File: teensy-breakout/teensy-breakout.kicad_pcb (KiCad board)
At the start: 6 copper layers, 240.5 x 168.5 mm, 103 parts, among them J1 USB_B, J10 1988820, J11 1988817, J12 1988817, J13 1988817, J14 1988817, J15 1988820, J17 1988956, J18 1988817, J19 1989010, J2 1988820, J20 1989010, J21 1988956, J22 1988817, J3 1988820, J4 1988820, J5 1988820, J6 1988820, J7 1988820, J8 1988833, J9 1988956, Q1 IRL530NSTRLPBF, SW1 7101MD9AQE, U1 Teensy4.1, U10 LSF0102DCUR, U3 FT232RL, U6 ICL7667CBAZA-TDKR, U7 LSF0102DCUR, U8 LSF0102DCUR

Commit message: Final silkscreen & testpoint touchups (still no images tho)
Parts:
- removed the REF** at (173.7, 121.1)
- added REF**: TestPoint_Pad_D1.5mm, TestPoint:TestPoint_Pad_D1.5mm, F.Cu at (94.0, 109.2)
- added REF**: PinHeader_1x02_P2.54mm_Vertical, Connector_PinHeader_2.54mm:PinHeader_1x02_P2.54mm_Vertical, F.Cu at (127.0, 179.1)
- added REF**: TestPoint_Pad_D1.5mm, TestPoint:TestPoint_Pad_D1.5mm, F.Cu at (78.7, 119.4)
- added REF**: TestPoint_Pad_D1.5mm, TestPoint:TestPoint_Pad_D1.5mm, F.Cu at (50.8, 119.4)
- added REF**: TestPoint_Pad_D1.5mm, TestPoint:TestPoint_Pad_D1.5mm, F.Cu at (185.4, 114.3)
- added REF**: TestPoint_Pad_D1.5mm, TestPoint:TestPoint_Pad_D1.5mm, F.Cu at (167.6, 114.3)
- added REF**: TestPoint_Pad_D1.5mm, TestPoint:TestPoint_Pad_D1.5mm, F.Cu at (45.7, 119.4)
- added REF**: TestPoint_Pad_D1.5mm, TestPoint:TestPoint_Pad_D1.5mm, F.Cu at (165.1, 114.3)
- added REF**: TestPoint_Pad_D1.5mm, TestPoint:TestPoint_Pad_D1.5mm, F.Cu at (182.9, 114.3)
- added REF**: TestPoint_Pad_D1.5mm, TestPoint:TestPoint_Pad_D1.5mm, F.Cu at (193.0, 114.3)
- added REF**: TestPoint_Pad_D1.5mm, TestPoint:TestPoint_Pad_D1.5mm, F.Cu at (200.7, 114.3)
- added REF**: TestPoint_Pad_D1.5mm, TestPoint:TestPoint_Pad_D1.5mm, F.Cu at (195.6, 114.3)
- added REF**: TestPoint_Pad_D1.5mm, TestPoint:TestPoint_Pad_D1.5mm, F.Cu at (71.1, 119.4)
- added REF**: TestPoint_Pad_D1.5mm, TestPoint:TestPoint_Pad_D1.5mm, F.Cu at (55.9, 119.4)
- added REF**: TestPoint_Pad_D1.5mm, TestPoint:TestPoint_Pad_D1.5mm, F.Cu at (188.0, 114.3)
- added REF**: TestPoint_Pad_D1.5mm, TestPoint:TestPoint_Pad_D1.5mm, F.Cu at (129.5, 175.3)
- added REF**: TestPoint_Pad_D1.5mm, TestPoint:TestPoint_Pad_D1.5mm, F.Cu at (160.0, 114.3)
- added REF**: TestPoint_Pad_D1.5mm, TestPoint:TestPoint_Pad_D1.5mm, F.Cu at (203.2, 114.3)
- added REF**: TestPoint_Pad_D1.5mm, TestPoint:TestPoint_Pad_D1.5mm, F.Cu at (81.3, 119.4)
- added REF**: TestPoint_Pad_D1.5mm, TestPoint:TestPoint_Pad_D1.5mm, F.Cu at (96.5, 109.2)
- added REF**: PinHeader_1x24_P2.54mm_Vertical, Connector_PinHeader_2.54mm:PinHeader_1x24_P2.54mm_Vertical, F.Cu at (147.4, 117.4)
- added REF**: TestPoint_Pad_D1.5mm, TestPoint:TestPoint_Pad_D1.5mm, F.Cu at (38.1, 119.4)
- added REF**: PinHeader_1x24_P2.54mm_Vertical, Connector_PinHeader_2.54mm:PinHeader_1x24_P2.54mm_Vertical, F.Cu at (38.1, 114.8)
- added REF**: TestPoint_Pad_D1.5mm, TestPoint:TestPoint_Pad_D1.5mm, F.Cu at (48.3, 119.4)
- added REF**: TestPoint_Pad_D1.5mm, TestPoint:TestPoint_Pad_D1.5mm, F.Cu at (88.9, 119.4)
- added REF**: TestPoint_Pad_D1.5mm, TestPoint:TestPoint_Pad_D1.5mm, F.Cu at (127.0, 175.3)
- added REF**: TestPoint_Pad_D1.5mm, TestPoint:TestPoint_Pad_D1.5mm, F.Cu at (154.9, 114.3)
- added REF**: TestPoint_Pad_D1.5mm, TestPoint:TestPoint_Pad_D1.5mm, F.Cu at (205.7, 114.3)
- added REF**: TestPoint_Pad_D1.5mm, TestPoint:TestPoint_Pad_D1.5mm, F.Cu at (83.8, 119.4)
- added REF**: TestPoint_Pad_D1.5mm, TestPoint:TestPoint_Pad_D1.5mm, F.Cu at (43.2, 119.4)
- added REF**: TestPoint_Pad_D1.5mm, TestPoint:TestPoint_Pad_D1.5mm, F.Cu at (152.4, 114.3)
- added REF**: TestPoint_Pad_D1.5mm, TestPoint:TestPoint_Pad_D1.5mm, F.Cu at (170.2, 114.3)
- added REF**: TestPoint_Pad_D1.5mm, TestPoint:TestPoint_Pad_D1.5mm, F.Cu at (73.7, 119.4)
- added REF**: TestPoint_Pad_D1.5mm, TestPoint:TestPoint_Pad_D1.5mm, F.Cu at (66.0, 119.4)
- added REF**: TestPoint_Pad_D1.5mm, TestPoint:TestPoint_Pad_D1.5mm, F.Cu at (58.4, 119.4)
- added REF**: TestPoint_Pad_D1.5mm, TestPoint:TestPoint_Pad_D1.5mm, F.Cu at (172.7, 114.3)
- added REF**: TestPoint_Pad_D1.5mm, TestPoint:TestPoint_Pad_D1.5mm, F.Cu at (198.1, 114.3)
- added REF**: TestPoint_Pad_D1.5mm, TestPoint:TestPoint_Pad_D1.5mm, F.Cu at (180.3, 114.3)
- added REF**: TestPoint_Pad_D1.5mm, TestPoint:TestPoint_Pad_D1.5mm, F.Cu at (149.9, 114.3)
- added REF**: TestPoint_Pad_D1.5mm, TestPoint:TestPoint_Pad_D1.5mm, F.Cu at (162.6, 114.3)
- added REF**: TestPoint_Pad_D1.5mm, TestPoint:TestPoint_Pad_D1.5mm, F.Cu at (91.4, 119.4)
- added REF**: TestPoint_Pad_D1.5mm, TestPoint:TestPoint_Pad_D1.5mm, F.Cu at (147.3, 114.3)
- added REF**: TestPoint_Pad_D1.5mm, TestPoint:TestPoint_Pad_D1.5mm, F.Cu at (53.3, 119.4)
- added REF**: TestPoint_Pad_D1.5mm, TestPoint:TestPoint_Pad_D1.5mm, F.Cu at (40.6, 119.4)
- added REF**: TestPoint_Pad_D1.5mm, TestPoint:TestPoint_Pad_D1.5mm, F.Cu at (177.8, 114.3)
- added REF**: TestPoint_Pad_D1.5mm, TestPoint:TestPoint_Pad_D1.5mm, F.Cu at (76.2, 119.4)
- added REF**: TestPoint_Pad_D1.5mm, TestPoint:TestPoint_Pad_D1.5mm, F.Cu at (175.3, 114.3)
- added REF**: TestPoint_Pad_D1.5mm, TestPoint:TestPoint_Pad_D1.5mm, F.Cu at (157.5, 114.3)
- added REF**: TestPoint_Pad_D1.5mm, TestPoint:TestPoint_Pad_D1.5mm, F.Cu at (61.0, 119.4)
- added REF**: TestPoint_Pad_D1.5mm, TestPoint:TestPoint_Pad_D1.5mm, F.Cu at (190.5, 114.3)
- added REF**: TestPoint_Pad_D1.5mm, TestPoint:TestPoint_Pad_D1.5mm, F.Cu at (68.6, 119.4)
- added REF**: TestPoint_Pad_D1.5mm, TestPoint:TestPoint_Pad_D1.5mm, F.Cu at (86.4, 119.4)
- added REF**: TestPoint_Pad_D1.5mm, TestPoint:TestPoint_Pad_D1.5mm, F.Cu at (63.5, 119.4)
- moved C12 15.9 mm to (44.5, 61.1), turned to -90 degrees
- moved C7 14.8 mm to (156.0, 96.7)
- moved C13 13.9 mm to (46.6, 61.0), turned to -90 degrees
- moved C20 7.92 mm to (156.0, 99.1)
- moved C9 7.75 mm to (45.6, 64.1)
- moved C23 3.30 mm to (125.2, 167.4)
- moved J5 0.23 mm to (16.6, 113.7)
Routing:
- net GND: track 737.3 -> 722.9 mm, vias 21 -> 16
- net Net-(D1-K): track 25.1 -> 37.5 mm
- net /LIM_R: track 148.6 -> 157.2 mm, vias 2 -> 1
- net /LIM_L: track 145.0 -> 153.6 mm, vias 2 -> 1
- net /UART1 CTS: track 185.8 -> 194.2 mm, vias 5 -> 4
- net /J0_4: track 190.4 -> 198.2 mm, vias 3 -> 2
- net /UART1 TX: track 196.3 -> 203.9 mm, vias 3 -> 2
- net /SCK1: track 224.1 -> 231.7 mm, vias 3 -> 2
- net /RF_CS: track 241.0 -> 248.6 mm, vias 3 -> 2
- net /NP3: track 231.0 -> 238.7 mm, vias 1 -> 0
- net /NP2: track 142.5 -> 150.1 mm, vias 3 -> 2
- net /MOSI1: track 220.4 -> 228.1 mm, vias 4 -> 3
- net /J0_3: track 198.7 -> 206.3 mm, vias 3 -> 2
- net /J0_2: track 222.0 -> 229.6 mm, vias 3 -> 2
- net /J0_1: track 223.4 -> 231.0 mm, vias 3 -> 2
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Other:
- board text added: "0"
- board text added: "1"
- board text added: "10"
- board text added: "14"
- board text added: "15"
- board text added: "18"
- board text added: "19"
- board text added: "2"
- board text added: "20"
- board text added: "22"
- board text added: "3"
- board text added: "34"
- board text added: "35"
- board text added: "36"
- board text added: "37"
- board text added: "40"
- board text added: "41"
- board text added: "9"
- board text added: "CS"
- board text added: "G0"
- board text added: "GPS Serial"
- board text added: "RST"
- board text added: "RX"
- board text added: "TX"

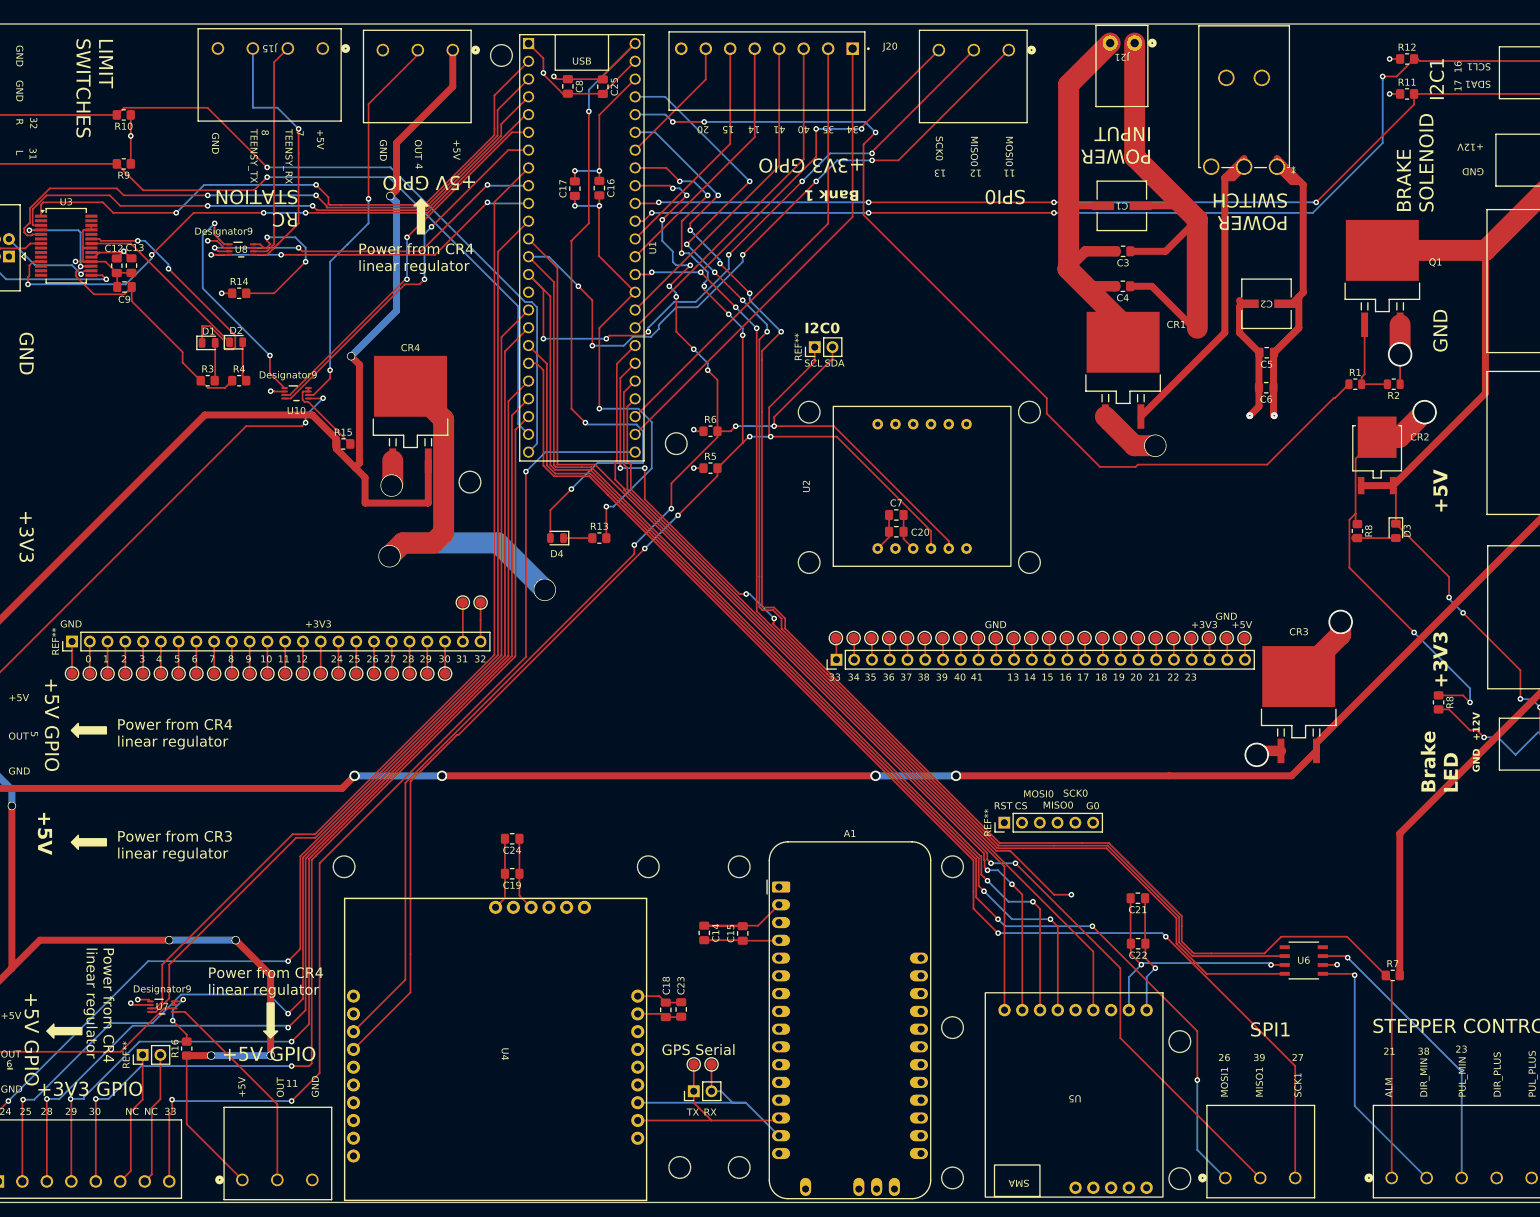
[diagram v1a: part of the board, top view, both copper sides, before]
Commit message: Changed mounting holes to use included M3 size
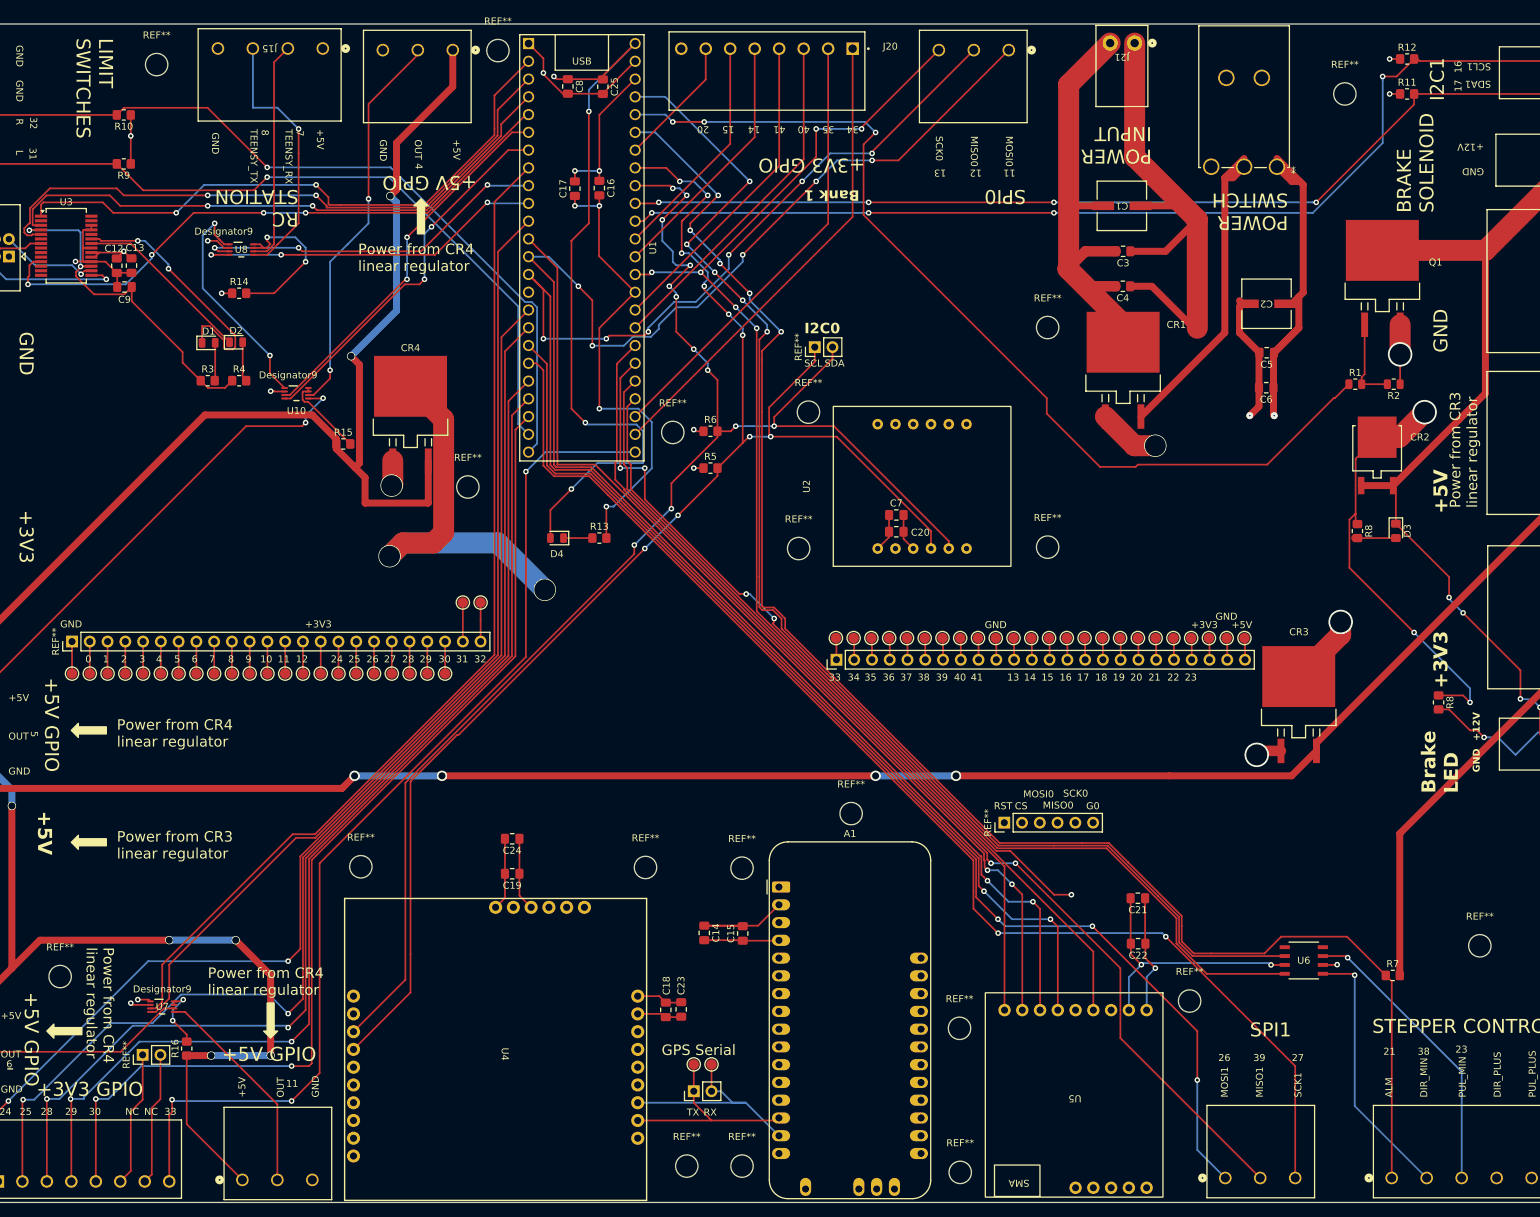
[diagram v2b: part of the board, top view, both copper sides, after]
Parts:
- removed ? (x17): , clipboard:fe42560d-e869-41d1-821b-38ac966b38b9
- added REF**: MountingHole_3.2mm_M3, MountingHole:MountingHole_3.2mm_M3, F.Cu at (220.1, 36.5)
- added REF**: MountingHole_3.2mm_M3, MountingHole:MountingHole_3.2mm_M3, F.Cu at (149.5, 139.4)
- added REF**: MountingHole_3.2mm_M3, MountingHole:MountingHole_3.2mm_M3, F.Cu at (126.0, 189.8)
- added REF**: MountingHole_3.2mm_M3, MountingHole:MountingHole_3.2mm_M3, F.Cu at (94.7, 92.7)
- added REF**: MountingHole_3.2mm_M3, MountingHole:MountingHole_3.2mm_M3, F.Cu at (133.9, 189.8)
- added REF**: MountingHole_3.2mm_M3, MountingHole:MountingHole_3.2mm_M3, F.Cu at (239.4, 158.3)
- added REF**: MountingHole_3.2mm_M3, MountingHole:MountingHole_3.2mm_M3, F.Cu at (197.9, 166.2)
- added REF**: MountingHole_3.2mm_M3, MountingHole:MountingHole_3.2mm_M3, F.Cu at (177.6, 69.9)
- added REF**: MountingHole_3.2mm_M3, MountingHole:MountingHole_3.2mm_M3, F.Cu at (142.0, 101.5)
- added REF**: MountingHole_3.2mm_M3, MountingHole:MountingHole_3.2mm_M3, F.Cu at (177.6, 101.3)
- added REF**: MountingHole_3.2mm_M3, MountingHole:MountingHole_3.2mm_M3, F.Cu at (120.1, 147.1)
- added REF**: MountingHole_3.2mm_M3, MountingHole:MountingHole_3.2mm_M3, F.Cu at (133.9, 147.2)
- added REF**: MountingHole_3.2mm_M3, MountingHole:MountingHole_3.2mm_M3, F.Cu at (143.4, 82.0)
- added REF**: MountingHole_3.2mm_M3, MountingHole:MountingHole_3.2mm_M3, F.Cu at (165.0, 170.1)
- added REF**: MountingHole_3.2mm_M3, MountingHole:MountingHole_3.2mm_M3, F.Cu at (36.4, 162.7)
- added REF**: MountingHole_3.2mm_M3, MountingHole:MountingHole_3.2mm_M3, F.Cu at (79.4, 147.0)
- added REF**: MountingHole_3.2mm_M3, MountingHole:MountingHole_3.2mm_M3, F.Cu at (50.2, 32.3)
- added REF**: MountingHole_3.2mm_M3, MountingHole:MountingHole_3.2mm_M3, F.Cu at (124.0, 84.9)
- added REF**: MountingHole_3.2mm_M3, MountingHole:MountingHole_3.2mm_M3, F.Cu at (99.0, 30.3)
- added REF**: MountingHole_3.2mm_M3, MountingHole:MountingHole_3.2mm_M3, F.Cu at (165.1, 190.7)
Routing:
- net /RF_CS: track 248.6 -> 231.3 mm
- net /MOSI0: track 341.4 -> 326.4 mm
- net /MISO0: track 330.3 -> 317.8 mm
- net GND: track 722.9 -> 723.7 mm

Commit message: Improved schematic layout, still in  progress
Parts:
- removed the J9 at (251.3, 127.6)
- removed the R8 at (233.5, 123.5)
- added J16: 1988956, Custom:CONN_1988956, F.Cu at (250.9, 125.4)
- added R17: 1k, Resistor_SMD:R_0805_2012Metric_Pad1.20x1.40mm_HandSolder, F.Cu at (234.6, 124.2)
- moved U1 176.9 mm to (99.1, 234.9)
- moved U2 157.9 mm to (61.0, 215.9)
- moved J1 155.3 mm to (33.9, 214.9)
- moved U3 155.3 mm to (42.1, 213.4), turned to 180 degrees
- moved REF** 150.4 mm to (114.3, 264.2), turned to 180 degrees
- moved U5 136.0 mm to (61.0, 242.6), turned to 90 degrees
- moved REF** 101.8 mm to (83.8, 205.7), turned to 0 degrees
- moved U4 79.2 mm to (144.8, 238.8)
- moved A1 77.4 mm to (172.7, 219.7)
- moved C14 4.86 mm to (133.3, 156.2)
- moved C24 4.32 mm to (101.0, 147.3)
- moved J18 3.14 mm to (158.8, 30.2)
- moved C15 1.92 mm to (135.9, 156.2)
- moved C19 1.86 mm to (101.0, 149.9)
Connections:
- J19 pad 7: /J0_7 -> +3V3
- J19 pad 8: /J0_8 -> GND
- J20 pad 8: unconnected-(J20-Pad8) -> GND
- U1 pad 25: /J0_8 -> /J0_6
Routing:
- net GND: track 723.7 -> 0.00 mm, vias 16 -> 0
- net +3V3: track 351.9 -> 0.00 mm, vias 11 -> 0
- net /ALM: track 343.2 -> 0.00 mm, vias 5 -> 0
- net /MOSI0: track 326.4 -> 0.00 mm, vias 7 -> 0
- net /I2C0_SCL: track 324.9 -> 0.00 mm, vias 10 -> 0
- net /I2C0_SDA: track 319.3 -> 0.00 mm, vias 12 -> 0
- net /MISO0: track 317.8 -> 0.00 mm, vias 8 -> 0
- net Net-(CR4-OUTPUT): track 315.6 -> 0.00 mm, vias 7 -> 0
- net /PUL: track 312.4 -> 0.00 mm, vias 5 -> 0
- net +5V: track 311.3 -> 0.00 mm, vias 8 -> 0
- net /SCK0: track 291.3 -> 0.00 mm, vias 7 -> 0
- net Net-(CR3-OUTPUT): track 284.5 -> 0.00 mm, vias 4 -> 0
- net /BRAKE: track 256.8 -> 0.00 mm, vias 3 -> 0
- net Net-(U1-16_A2_RX4_SCL1): track 248.6 -> 0.00 mm, vias 4 -> 0
- net Net-(U1-17_A3_TX4_SDA1): track 241.7 -> 0.00 mm, vias 4 -> 0
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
